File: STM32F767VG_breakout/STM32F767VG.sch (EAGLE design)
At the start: 43 parts, among them IC1 STM32F767VGT6, IC2 L7805CV, IC3 LD117AS33TR, X4 8MHz, X5 32.768kHz

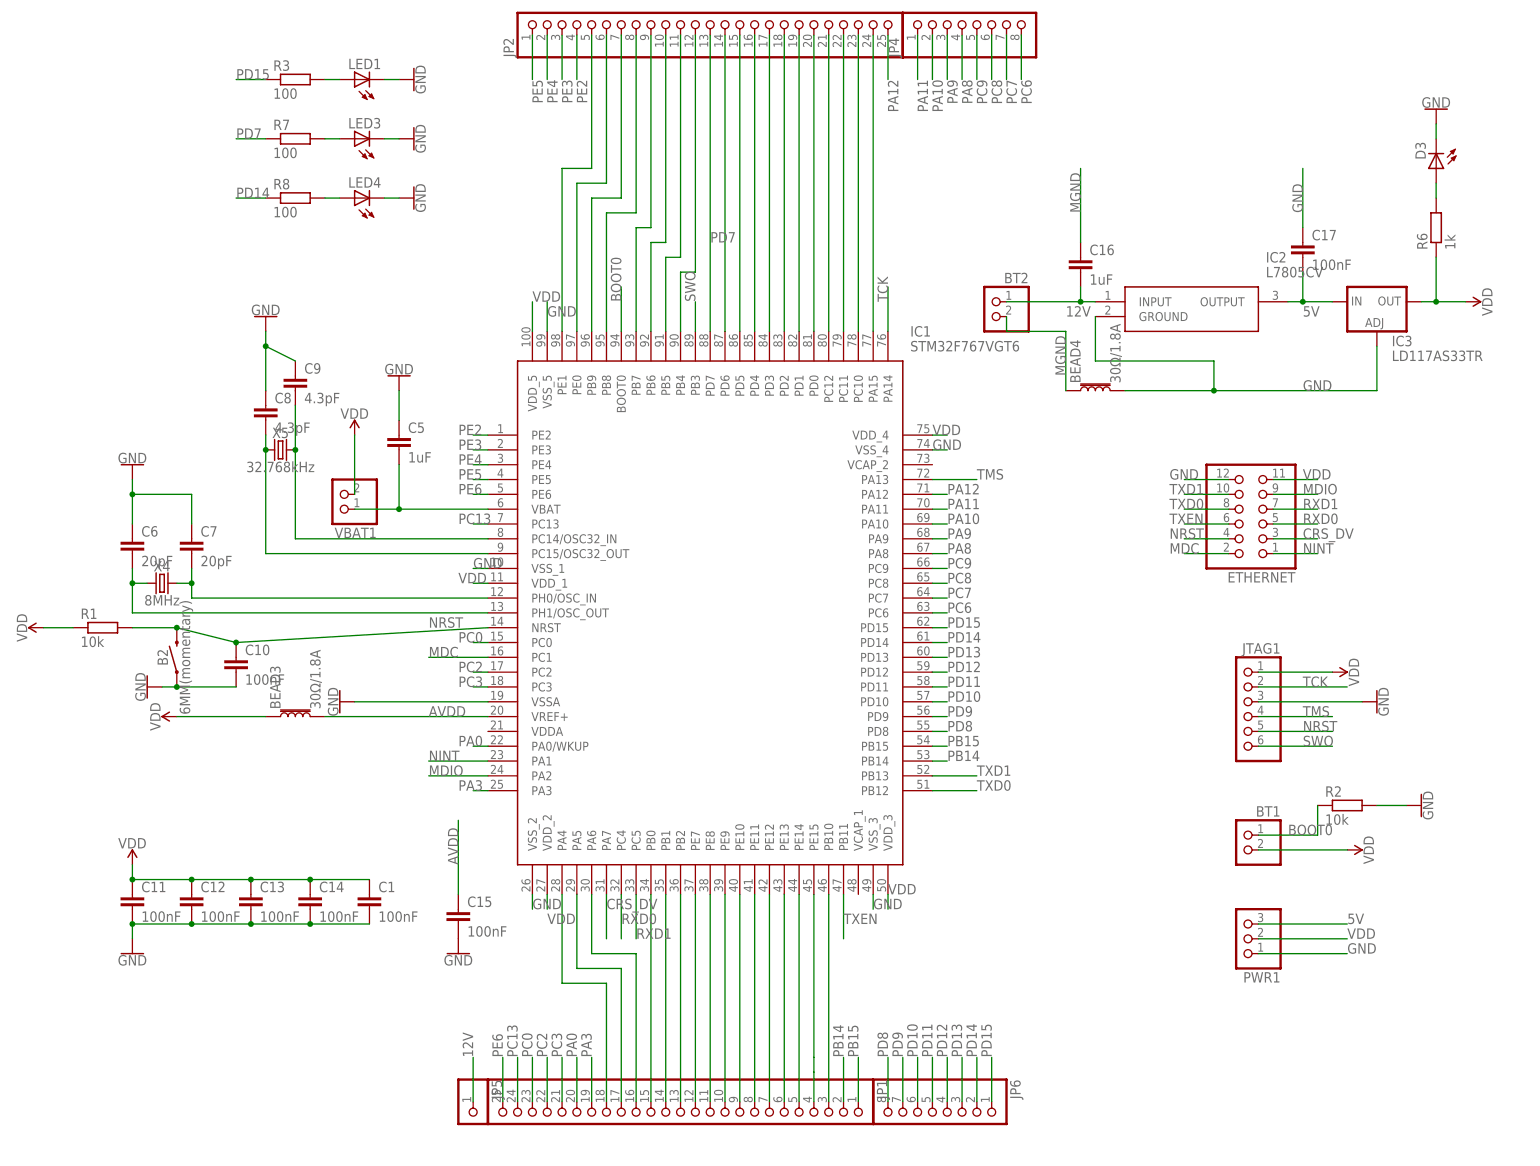
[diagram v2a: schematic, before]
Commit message: Replacement
Rotated the microcontroller. Will route the side pins later.
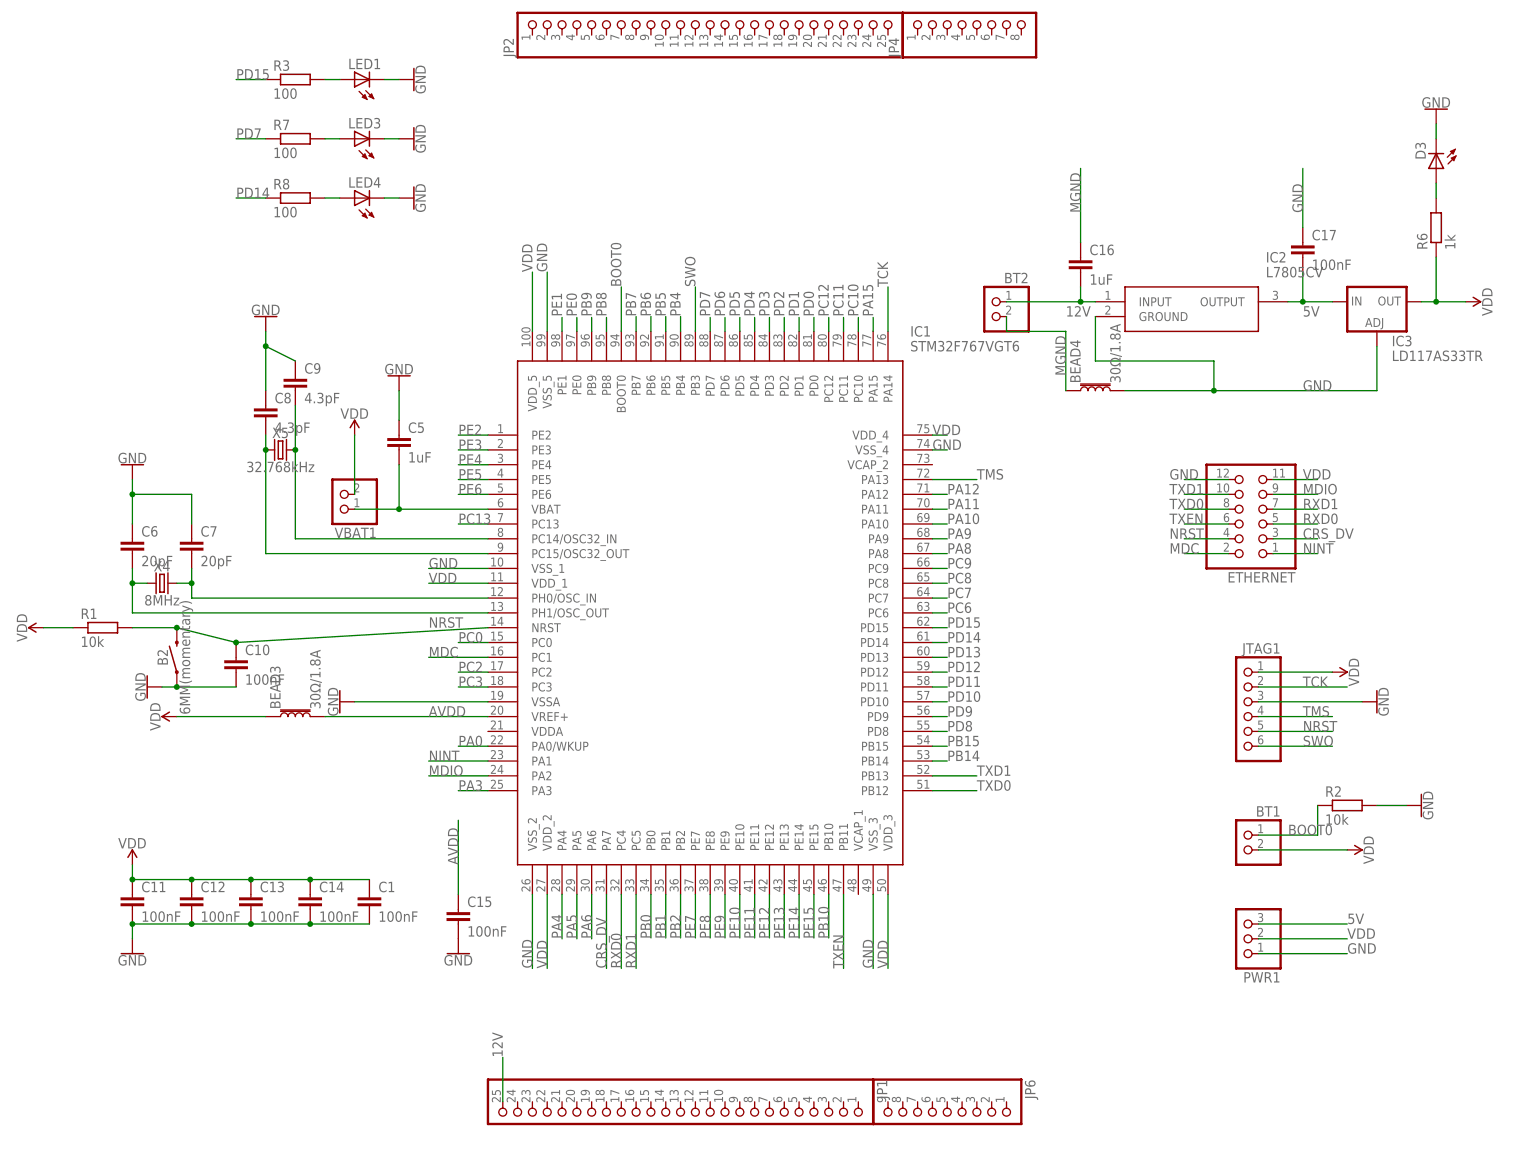
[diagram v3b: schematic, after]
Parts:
- removed JP5: (no value), pinhead:PINHD-1X1
- JP6: device pinhead:PINHD-1X8 -> pinhead:PINHD-1X9
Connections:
- removed net N$1: IC1.PB10, JP1.3
- removed net N$10: IC1.PE7, JP1.12
- removed net N$11: IC1.PB2, JP1.13
- removed net N$12: IC1.PB1, JP1.14
- removed net N$18: IC1.PB0, JP1.15
- removed net N$2: IC1.PE15, JP1.4
- removed net N$20: IC1.PA6, JP1.16
- removed net N$24: IC1.PA5, JP1.17
- removed net N$25: IC1.PA4, JP1.18
- removed net N$3: IC1.PE14, JP1.5
- removed net N$33: IC1.PB6, JP2.10
- removed net N$34: IC1.PB7, JP2.9
- removed net N$35: IC1.PB8, JP2.8
- removed net N$36: IC1.PB9, JP2.7
- removed net N$37: IC1.PE0, JP2.6
- removed net N$4: IC1.PE13, JP1.6
- removed net N$43: IC1.PD3, JP2.17
- removed net N$45: IC1.PD1, JP2.19
- removed net N$48: IC1.PC11, JP2.22
- removed net N$49: IC1.PC10, JP2.23
- removed net N$5: IC1.PE12, JP1.7
- removed net N$50: IC1.PA15, JP2.24
- removed net N$58: IC1.PD6, JP2.14
- removed net N$59: IC1.PD5, JP2.15
- removed net N$6: IC1.PE11, JP1.8
- removed net N$60: IC1.PD4, JP2.16
- removed net N$64: IC1.PC12, JP2.21
- removed net N$65: IC1.PD0, JP2.20
- removed net N$67: IC1.PD2, JP2.18
- removed net N$7: IC1.PE10, JP1.9
- removed net N$71: IC1.PB5, JP2.11
- removed net N$72: IC1.PB4, JP2.12
- removed net N$8: IC1.PE9, JP1.10
- removed net N$9: IC1.PE8, JP1.11
- new net PA15: IC1.PA15
- new net PA4: IC1.PA4
- new net PA5: IC1.PA5
- new net PA6: IC1.PA6
- new net PB0: IC1.PB0
- new net PB1: IC1.PB1
- new net PB10: IC1.PB10
- new net PB2: IC1.PB2
- new net PB4: IC1.PB4
- new net PB5: IC1.PB5
- new net PB6: IC1.PB6
- new net PB7: IC1.PB7
- new net PB8: IC1.PB8
- new net PB9: IC1.PB9
- new net PC10: IC1.PC10
- new net PC11: IC1.PC11
- new net PC12: IC1.PC12
- new net PD0: IC1.PD0
- new net PD1: IC1.PD1
- new net PD2: IC1.PD2
- new net PD3: IC1.PD3
- new net PD4: IC1.PD4
- new net PD5: IC1.PD5
- new net PD6: IC1.PD6
- new net PE0: IC1.PE0
- new net PE1: IC1.PE1
- new net PE10: IC1.PE10
- new net PE11: IC1.PE11
- new net PE12: IC1.PE12
- new net PE13: IC1.PE13
- new net PE14: IC1.PE14
- new net PE15: IC1.PE15
- new net PE7: IC1.PE7
- new net PE8: IC1.PE8
- new net PE9: IC1.PE9
- net 12V: now also JP1.25; no longer JP5.1
- net PA0: no longer JP1.20
- net PA10: no longer JP4.2
- net PA11: no longer JP4.1
- net PA12: no longer JP2.25
- net PA3: no longer JP1.19
- net PA8: no longer JP4.4
- net PA9: no longer JP4.3
- net PB14: no longer JP1.2
- net PB15: no longer JP1.1
- net PC0: no longer JP1.23
- net PC13: no longer JP1.24
- net PC2: no longer JP1.22
- net PC3: no longer JP1.21
- net PC6: no longer JP4.8
- net PC7: no longer JP4.7
- net PC8: no longer JP4.6
- net PC9: no longer JP4.5
- net PD10: no longer JP6.6
- net PD11: no longer JP6.5
- net PD12: no longer JP6.4
- net PD13: no longer JP6.3
- net PD14: no longer JP6.2
- net PD15: no longer JP6.1
- net PD7: no longer JP2.13
- net PD8: no longer JP6.8
- net PD9: no longer JP6.7
- net PE2: no longer IC1.PE1, JP2.4, JP2.5
- net PE3: no longer JP2.3
- net PE4: no longer JP2.2
- net PE5: no longer JP2.1
- net PE6: no longer JP1.25

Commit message: Ethernet and Crystal Rounting
First draft of ethernet and crystal routing. If ok, then will move on to sid epin headers
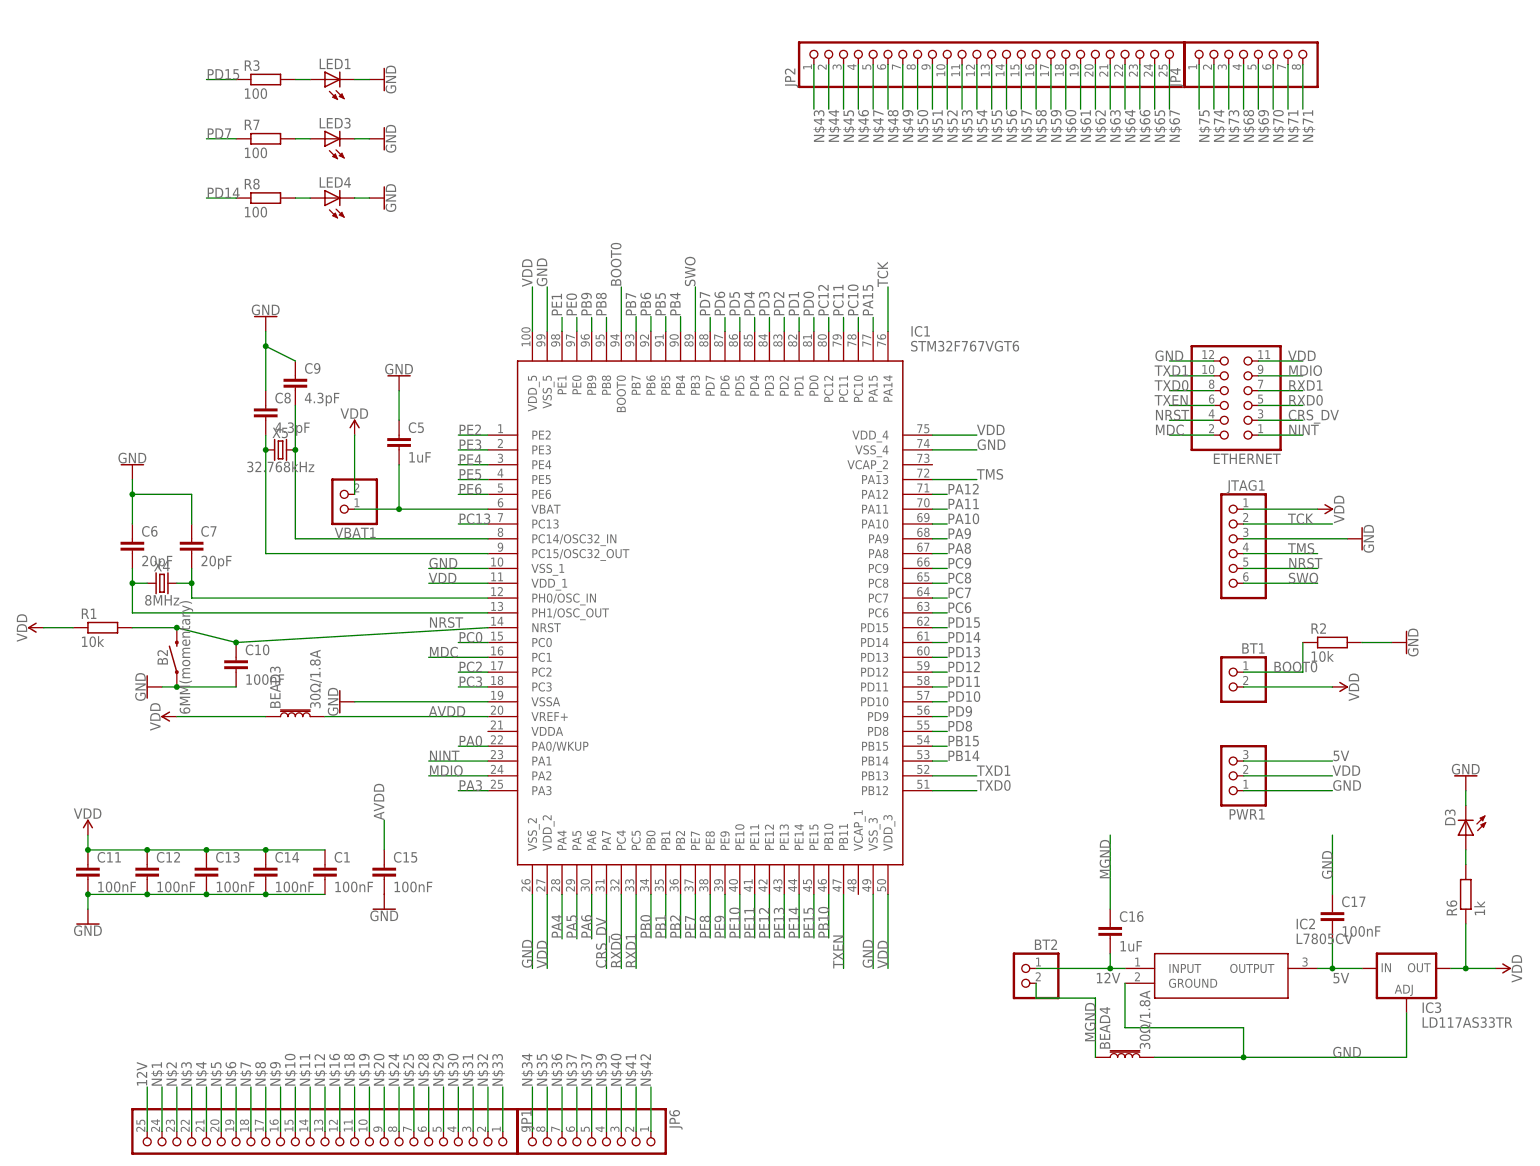
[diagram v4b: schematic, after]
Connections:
- new net N$1: JP1.24
- new net N$10: JP1.15
- new net N$11: JP1.14
- new net N$12: JP1.13
- new net N$16: JP1.12
- new net N$18: JP1.11
- new net N$19: JP1.10
- new net N$2: JP1.23
- new net N$20: JP1.9
- new net N$24: JP1.8
- new net N$25: JP1.7
- new net N$28: JP1.6
- new net N$29: JP1.5
- new net N$3: JP1.22
- new net N$30: JP1.4
- new net N$31: JP1.3
- new net N$32: JP1.2
- new net N$33: JP1.1
- new net N$34: JP6.9
- new net N$35: JP6.8
- new net N$36: JP6.7
- new net N$37: JP6.6
- new net N$38: JP6.5
- new net N$39: JP6.4
- new net N$4: JP1.21
- new net N$40: JP6.3
- new net N$41: JP6.2
- new net N$42: JP6.1
- new net N$43: JP2.1
- new net N$44: JP2.2
- new net N$45: JP2.3
- new net N$46: JP2.4
- new net N$47: JP2.5
- new net N$48: JP2.6
- new net N$49: JP2.7
- new net N$5: JP1.20
- new net N$50: JP2.8
- new net N$51: JP2.9
- new net N$52: JP2.10
- new net N$53: JP2.11
- new net N$54: JP2.12
- new net N$55: JP2.13
- new net N$56: JP2.14
- new net N$57: JP2.15
- new net N$58: JP2.16
- new net N$59: JP2.17
- new net N$6: JP1.19
- new net N$60: JP2.18
- new net N$61: JP2.19
- new net N$62: JP2.20
- new net N$63: JP2.21
- new net N$64: JP2.22
- new net N$65: JP2.24
- new net N$66: JP2.23
- new net N$67: JP2.25
- new net N$68: JP4.4
- new net N$69: JP4.5
- new net N$7: JP1.18
- new net N$70: JP4.6
- new net N$71: JP4.7
- new net N$72: JP4.8
- new net N$73: JP4.3
- new net N$74: JP4.2
- new net N$75: JP4.1
- new net N$8: JP1.17
- new net N$9: JP1.16
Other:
- moved on the sheet: BEAD4, BT1, BT2, C1, C11, C12, C13, C14, C15, C16, C17, D3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
